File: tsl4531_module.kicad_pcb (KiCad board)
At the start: 2 copper layers, 13.2 x 16.5 mm, 3 parts

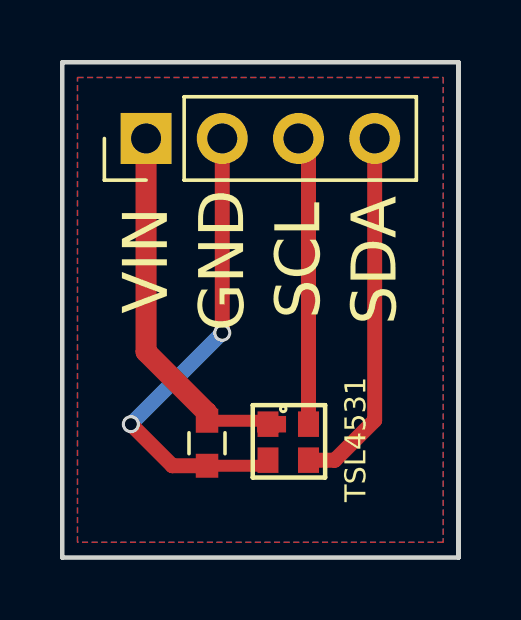
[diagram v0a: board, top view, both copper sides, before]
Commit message: Remove unnecessary tracks and vias
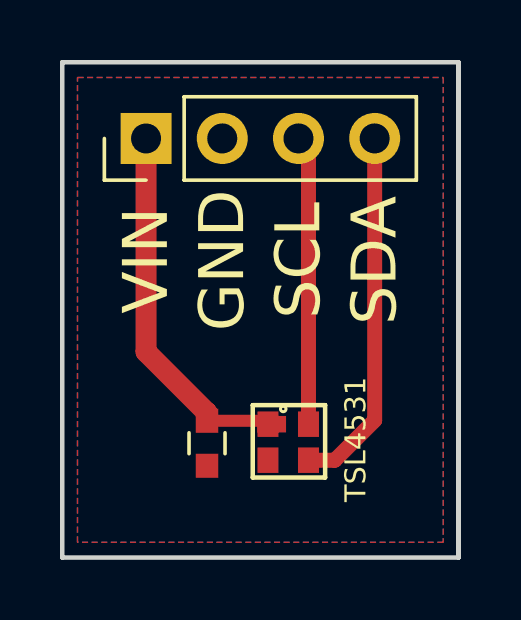
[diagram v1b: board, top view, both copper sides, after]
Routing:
- net GND: track 16.3 -> 0.00 mm, vias 2 -> 0
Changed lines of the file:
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@@
     (thickness 1.6)
     (drawings 10)
-    (tracks 21)
+    (tracks 12)
     (zones 0)
     (modules 3)
@@
     (pad_to_mask_clearance 0)
     (aux_axis_origin 0 0)
-    (visible_elements FFFFFF7F)
+    (visible_elements FFFFFF5F)
     (pcbplotparams
       (layerselection 0x00030_80000001)
@@
   (segment (start 150.876 96.52) (end 150.876 103.632) (width 0.7) (layer F.Cu) (net 1))
   (segment (start 154.825 105.93) (end 154.94 106.045) (width 0.25) (layer F.Cu) (net 1))
-  (segment (start 150.368 106.045) (end 153.416 102.997) (width 0.5) (layer B.Cu) (net 2))
-  (segment (start 151.753 107.43) (end 150.368 106.045) (width 0.5) (layer F.Cu) (net 2))
-  (via (at 150.368 106.045) (size 0.6) (drill 0.4) (layers F.Cu B.Cu) (net 2))
-  (segment (start 152.908 107.43) (end 151.753 107.43) (width 0.5) (layer F.Cu) (net 2))
-  (segment (start 153.416 102.997) (end 153.416 96.52) (width 0.5) (layer F.Cu) (net 2))
-  (via (at 153.416 102.997) (size 0.6) (drill 0.4) (layers F.Cu B.Cu) (net 2))
-  (segment (start 152.908 107.43) (end 154.755 107.43) (width 0.4) (layer F.Cu) (net 2))
-  (segment (start 154.755 107.43) (end 154.94 107.245) (width 0.4) (layer F.Cu) (net 2))
-  (segment (start 154.755 107.43) (end 154.94 107.245) (width 0.25) (layer F.Cu) (net 2))
   (segment (start 158.496 96.52) (end 158.496 105.918) (width 0.5) (layer F.Cu) (net 3))
   (segment (start 157.169 107.245) (end 158.496 105.918) (width 0.5) (layer F.Cu) (net 3))
